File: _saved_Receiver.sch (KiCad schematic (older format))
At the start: 25 parts, among them U1 TL074 (ggf. durch TLV4172IPWR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

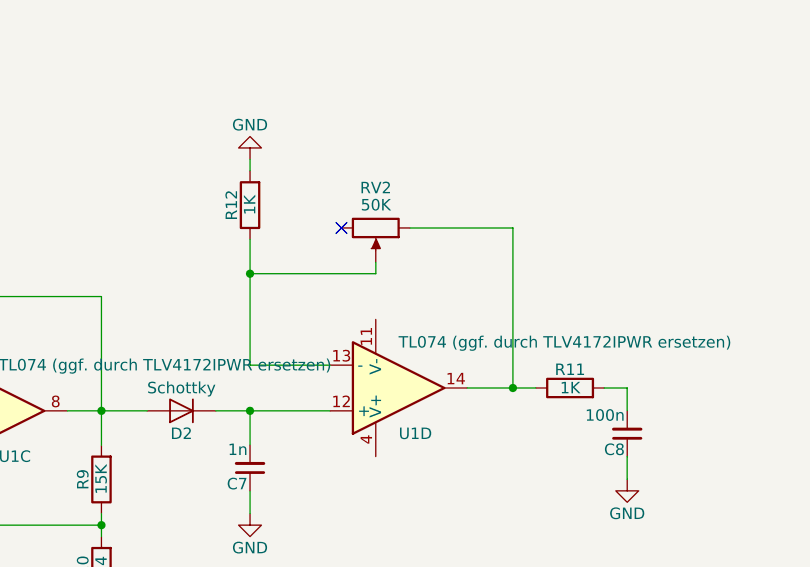
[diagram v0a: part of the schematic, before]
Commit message: Add files via upload
Netzliste erstellt und Anfang von Layout
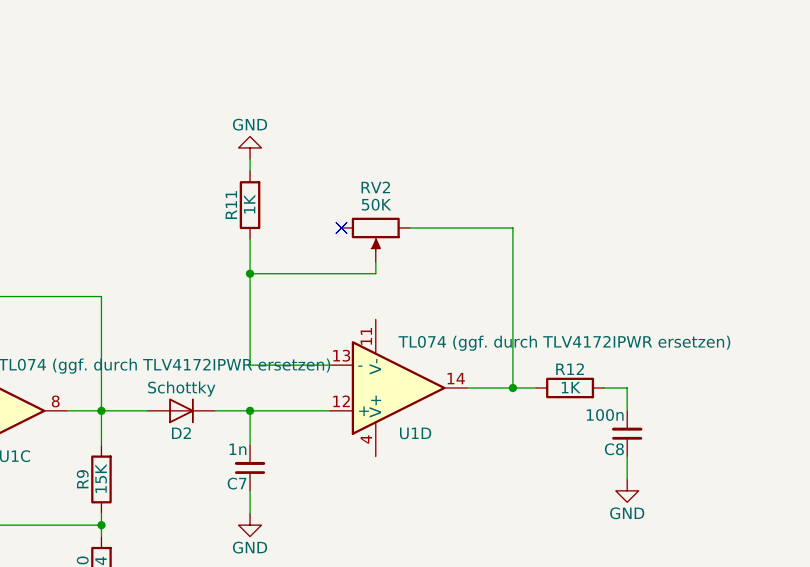
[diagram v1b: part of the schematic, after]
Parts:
- C1, C2, C3, C4, C5, C6, C7, C8: footprint Capacitors_SMD:C_0603 -> Capacitor_SMD:C_0603_1608Metric
- D1: footprint Opto-Devices:PhotoDiode_DIL2_4.3x4.65_RM5.08 -> OptoDevice:Osram_DIL2_4.3x4.65mm_P5.08mm
- D2: footprint Diodes_SMD:D_SOD-123 -> Diode_SMD:D_SOD-123
- R1, R10, R2, R3, R4, R5, R6, R7, R8, R9: footprint Resistors_SMD:R_0603 -> Resistor_SMD:R_0603_1608Metric
- R11: renamed from R12; footprint Resistors_SMD:R_0603 -> Resistor_SMD:R_0603_1608Metric
- R12: renamed from R11; footprint Resistors_SMD:R_0603 -> Resistor_SMD:R_0603_1608Metric
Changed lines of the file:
@@
 F 0 "D1" H 3170 3370 50  0000 L CNN
 F 1 "BPW34" H 3110 3190 50  0000 C CNN
-F 2 "Opto-Devices:PhotoDiode_DIL2_4.3x4.65_RM5.08" H 3150 3475 50  0001 C CNN
+F 2 "OptoDevice:Osram_DIL2_4.3x4.65mm_P5.08mm" H 3150 3475 50  0001 C CNN
 F 3 "" H 3100 3300 50  0001 C CNN
 	1    3150 3300
@@
 F 0 "R1" V 4730 3700 50  0000 C CNN
 F 1 "75K" V 4650 3700 50  0000 C CNN
-F 2 "Resistors_SMD:R_0603" V 4580 3700 50  0001 C CNN
+F 2 "Resistor_SMD:R_0603_1608Metric" V 4580 3700 50  0001 C CNN
 F 3 "" H 4650 3700 50  0001 C CNN
 	1    4650 3700
@@
 F 0 "R2" V 4980 3950 50  0000 C CNN
 F 1 "1K02" V 4900 3950 50  0000 C CNN
-F 2 "Resistors_SMD:R_0603" V 4830 3950 50  0001 C CNN
+F 2 "Resistor_SMD:R_0603_1608Metric" V 4830 3950 50  0001 C CNN
 F 3 "" H 4900 3950 50  0001 C CNN
 	1    4900 3950
@@
 F 0 "C4" H 5210 3770 50  0000 L CNN
 F 1 "390p" H 5210 3620 50  0000 L CNN
-F 2 "Capacitors_SMD:C_0603" H 5200 3700 50  0001 C CNN
+F 2 "Capacitor_SMD:C_0603_1608Metric" H 5200 3700 50  0001 C CNN
 F 3 "" H 5200 3700 50  0001 C CNN
 	1    5200 3700
@@
 F 0 "C3" H 5210 3370 50  0000 L CNN
 F 1 "390p" H 5210 3220 50  0000 L CNN
-F 2 "Capacitors_SMD:C_0603" H 5200 3300 50  0001 C CNN
+F 2 "Capacitor_SMD:C_0603_1608Metric" H 5200 3300 50  0001 C CNN
 F 3 "" H 5200 3300 50  0001 C CNN
 	1    5200 3300
@@
 F 0 "R3" V 5530 3500 50  0000 C CNN
 F 1 "102K" V 5450 3500 50  0000 C CNN
-F 2 "Resistors_SMD:R_0603" V 5380 3500 50  0001 C CNN
+F 2 "Resistor_SMD:R_0603_1608Metric" V 5380 3500 50  0001 C CNN
 F 3 "" H 5450 3500 50  0001 C CNN
 	1    5450 3500
@@
 F 0 "R4" V 6430 4100 50  0000 C CNN
 F 1 "15K4" V 6350 4100 50  0000 C CNN
-F 2 "Resistors_SMD:R_0603" V 6280 4100 50  0001 C CNN
+F 2 "Resistor_SMD:R_0603_1608Metric" V 6280 4100 50  0001 C CNN
 F 3 "" H 6350 4100 50  0001 C CNN
 	1    6350 4100
@@
 F 0 "R5" V 6430 4500 50  0000 C CNN
 F 1 "249" V 6350 4500 50  0000 C CNN
-F 2 "Resistors_SMD:R_0603" V 6280 4500 50  0001 C CNN
+F 2 "Resistor_SMD:R_0603_1608Metric" V 6280 4500 50  0001 C CNN
 F 3 "" H 6350 4500 50  0001 C CNN
 	1    6350 4500
@@
 F 0 "R6" V 6780 3800 50  0000 C CNN
 F 1 "49K9" V 6700 3800 50  0000 C CNN
-F 2 "Resistors_SMD:R_0603" V 6630 3800 50  0001 C CNN
+F 2 "Resistor_SMD:R_0603_1608Metric" V 6630 3800 50  0001 C CNN
 F 3 "" H 6700 3800 50  0001 C CNN
 	1    6700 3800
@@
 F 0 "R7" V 7030 4050 50  0000 C CNN
 F 1 "976" V 6950 4050 50  0000 C CNN
-F 2 "Resistors_SMD:R_0603" V 6880 4050 50  0001 C CNN
+F 2 "Resistor_SMD:R_0603_1608Metric" V 6880 4050 50  0001 C CNN
 F 3 "" H 6950 4050 50  0001 C CNN
 	1    6950 4050
@@
 F 0 "C6" H 7260 3870 50  0000 L CNN
 F 1 "390p" H 7260 3720 50  0000 L CNN
-F 2 "Capacitors_SMD:C_0603" H 7250 3800 50  0001 C CNN
+F 2 "Capacitor_SMD:C_0603_1608Metric" H 7250 3800 50  0001 C CNN
 F 3 "" H 7250 3800 50  0001 C CNN
 	1    7250 3800
@@
 F 0 "C5" H 7260 3470 50  0000 L CNN
 F 1 "390p" H 7260 3320 50  0000 L CNN
-F 2 "Capacitors_SMD:C_0603" H 7250 3400 50  0001 C CNN
+F 2 "Capacitor_SMD:C_0603_1608Metric" H 7250 3400 50  0001 C CNN
 F 3 "" H 7250 3400 50  0001 C CNN
 	1    7250 3400
@@
 F 0 "R8" V 7580 3600 50  0000 C CNN
 F 1 "97K6" V 7500 3600 50  0000 C CNN
-F 2 "Resistors_SMD:R_0603" V 7430 3600 50  0001 C CNN
+F 2 "Resistor_SMD:R_0603_1608Metric" V 7430 3600 50  0001 C CNN
 F 3 "" H 7500 3600 50  0001 C CNN
 	1    7500 3600
@@
 F 0 "R9" V 8480 4200 50  0000 C CNN
 F 1 "15K" V 8400 4200 50  0000 C CNN
-F 2 "Resistors_SMD:R_0603" V 8330 4200 50  0001 C CNN
+F 2 "Resistor_SMD:R_0603_1608Metric" V 8330 4200 50  0001 C CNN
 F 3 "" H 8400 4200 50  0001 C CNN
 	1    8400 4200
@@
 F 0 "R10" V 8480 4600 50  0000 C CNN
 F 1 "274" V 8400 4600 50  0000 C CNN
-F 2 "Resistors_SMD:R_0603" V 8330 4600 50  0001 C CNN
+F 2 "Resistor_SMD:R_0603_1608Metric" V 8330 4600 50  0001 C CNN
 F 3 "" H 8400 4600 50  0001 C CNN
 	1    8400 4600
@@
 F 0 "C1" H 2410 2670 50  0000 L CNN
 F 1 "100n 50V" H 2410 2520 50  0000 L CNN
-F 2 "Capacitors_SMD:C_0603" H 2400 2600 50  0001 C CNN
+F 2 "Capacitor_SMD:C_0603_1608Metric" H 2400 2600 50  0001 C CNN
 F 3 "" H 2400 2600 50  0001 C CNN
 	1    2400 2600
@@
 F 0 "D2" H 8750 4000 50  0000 C CNN
 F 1 "Schottky " H 8750 3800 50  0000 C CNN
-F 2 "Diodes_SMD:D_SOD-123" H 8750 3900 50  0001 C CNN
+F 2 "Diode_SMD:D_SOD-123" H 8750 3900 50  0001 C CNN
 F 3 "" H 8750 3900 50  0001 C CNN
 	1    8750 3900
@@
 F 0 "C7" H 9060 4220 50  0000 L CNN
 F 1 "1n" H 9060 4070 50  0000 L CNN
-F 2 "Capacitors_SMD:C_0603" H 9050 4150 50  0001 C CNN
+F 2 "Capacitor_SMD:C_0603_1608Metric" H 9050 4150 50  0001 C CNN
 F 3 "" H 9050 4150 50  0001 C CNN
 	1    9050 4150
@@
 $EndComp
 $Comp
-L power:GND #PWR011
+L power:GND #PWR012
 U 1 1 5AEB0733
 P 9050 4350
-F 0 "#PWR011" H 9050 4100 50  0001 C CNN
+F 0 "#PWR012" H 9050 4100 50  0001 C CNN
 F 1 "GND" H 9050 4200 50  0000 C CNN
 F 2 "" H 9050 4350 50  0001 C CNN
@@
 	10000 3800 10200 3800
 $Comp
-L device:R R11
+L device:R R12
 U 1 1 5AEB0CD1
 P 10450 3800
-F 0 "R11" V 10530 3800 50  0000 C CNN
+F 0 "R12" V 10530 3800 50  0000 C CNN
 F 1 "1K" V 10450 3800 50  0000 C CNN
-F 2 "Resistors_SMD:R_0603" V 10380 3800 50  0001 C CNN
+F 2 "Resistor_SMD:R_0603_1608Metric" V 10380 3800 50  0001 C CNN
 F 3 "" H 10450 3800 50  0001 C CNN
 	1    10450 3800
@@
 F 0 "C8" H 10710 4070 50  0000 L CNN
 F 1 "100n" H 10710 3920 50  0000 L CNN
-F 2 "Capacitors_SMD:C_0603" H 10700 4000 50  0001 C CNN
+F 2 "Capacitor_SMD:C_0603_1608Metric" H 10700 4000 50  0001 C CNN
 F 3 "" H 10700 4000 50  0001 C CNN
 	1    10700 4000
@@
 	10700 3800 10600 3800
 $Comp
-L power:GND #PWR012
+L power:GND #PWR013
 U 1 1 5AEB0E88
 P 10700 4200
-F 0 "#PWR012" H 10700 3950 50  0001 C CNN
+F 0 "#PWR013" H 10700 3950 50  0001 C CNN
 F 1 "GND" H 10700 4050 50  0000 C CNN
 F 2 "" H 10700 4200 50  0001 C CNN
@@
 	3600 3150 3600 3600
 $Comp
-L power:GND #PWR0101
+L power:GND #PWR04
 U 1 1 5AF8AD6F
 P 3600 4050
-F 0 "#PWR0101" H 3600 3800 50  0001 C CNN
+F 0 "#PWR04" H 3600 3800 50  0001 C CNN
 F 1 "GND" H 3600 3900 50  0000 C CNN
 F 2 "" H 3600 4050 50  0001 C CNN
@@
 	3600 3800 3700 3800
 $Comp
-L power:+12V #PWR0102
+L power:+12V #PWR03
 U 1 1 5AF8CCE8
 P 3150 3000
-F 0 "#PWR0102" H 3150 2850 50  0001 C CNN
+F 0 "#PWR03" H 3150 2850 50  0001 C CNN
 F 1 "+12V" H 3150 3140 50  0000 C CNN
 F 2 "" H 3150 3000 50  0001 C CNN
@@
 	3150 3600 3600 3600
 $Comp
-L device:R R12
+L device:R R11
 U 1 1 5AF96B45
 P 9050 3000
-F 0 "R12" V 9130 3000 50  0000 C CNN
+F 0 "R11" V 9130 3000 50  0000 C CNN
 F 1 "1K" V 9050 3000 50  0000 C CNN
-F 2 "Resistors_SMD:R_0603" V 8980 3000 50  0001 C CNN
+F 2 "Resistor_SMD:R_0603_1608Metric" V 8980 3000 50  0001 C CNN
 F 3 "" H 9050 3000 50  0001 C CNN
 	1    9050 3000
@@
 $EndComp
 $Comp
-L power:GND #PWR0103
+L power:GND #PWR011
 U 1 1 5AF98829
 P 9050 2800
-F 0 "#PWR0103" H 9050 2550 50  0001 C CNN
+F 0 "#PWR011" H 9050 2550 50  0001 C CNN
 F 1 "GND" H 9050 2650 50  0000 C CNN
 F 2 "" H 9050 2800 50  0001 C CNN
@@
 F 0 "C2" H 2810 2670 50  0000 L CNN
 F 1 "1u 50V" H 2810 2520 50  0000 L CNN
-F 2 "Capacitors_SMD:C_0603" H 2800 2600 50  0001 C CNN
+F 2 "Capacitor_SMD:C_0603_1608Metric" H 2800 2600 50  0001 C CNN
 F 3 "" H 2800 2600 50  0001 C CNN
 	1    2800 2600
